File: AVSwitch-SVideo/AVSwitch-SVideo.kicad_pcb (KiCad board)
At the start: 2 copper layers, 100 x 100 mm, 9 parts, among them J1 Conn_01x35_Pin, J4 Mini-DIN-4, U1 SN74CBT3244PW

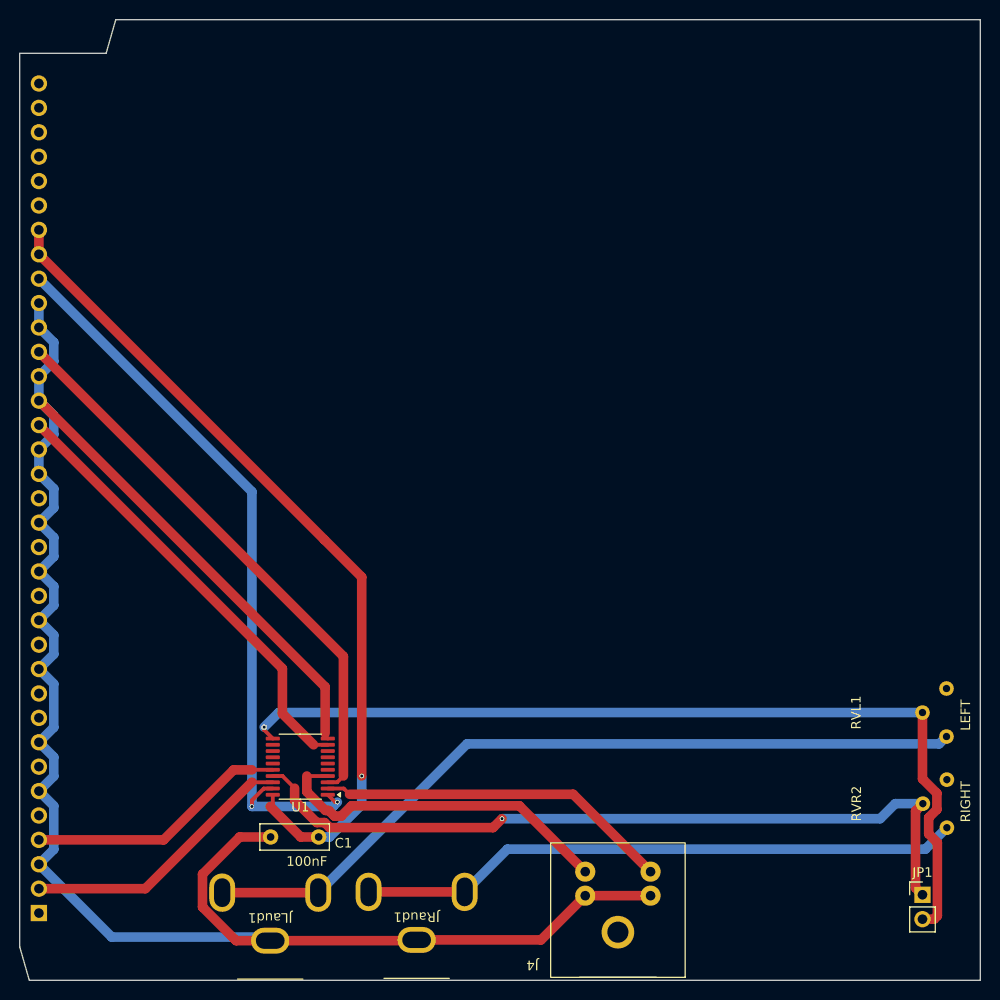
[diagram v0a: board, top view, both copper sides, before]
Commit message: Add files via upload
New version with better footprint and ground isolation.
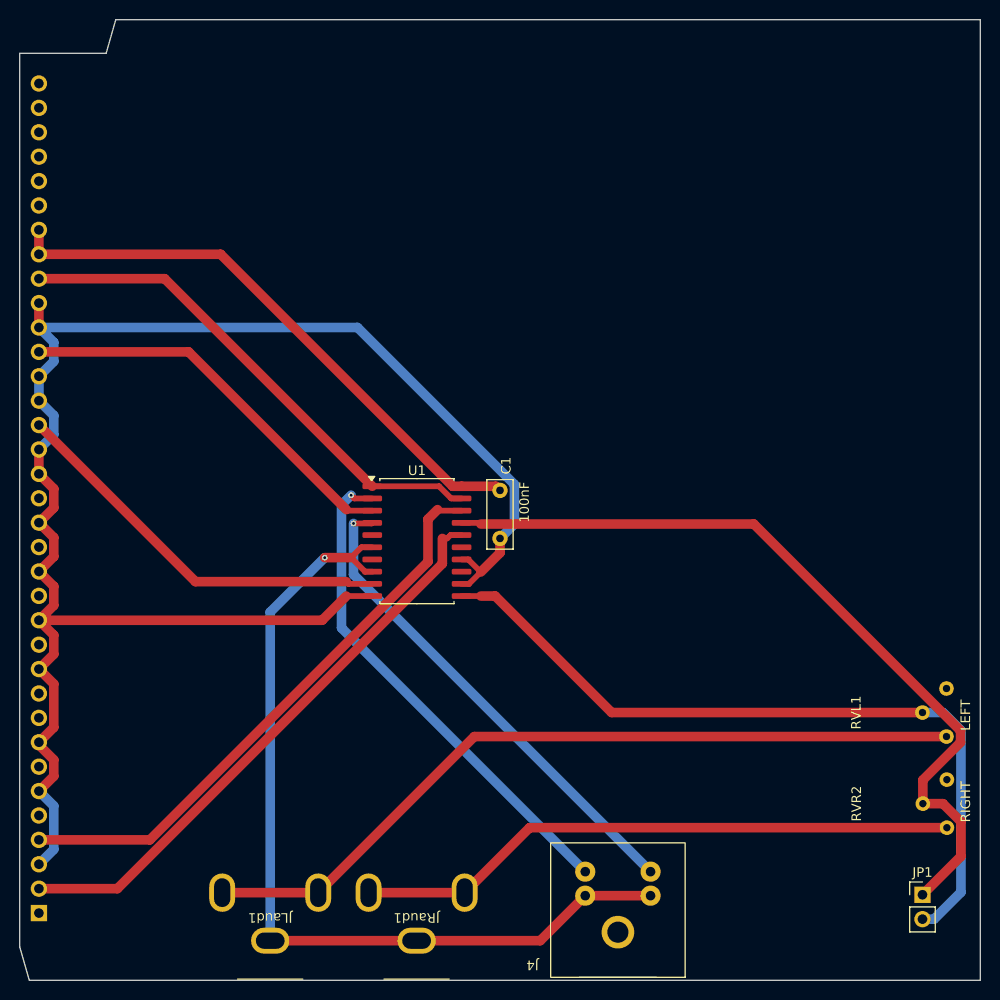
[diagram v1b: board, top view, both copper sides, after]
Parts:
- U1: footprint Package_SO:TSSOP-20_4.4x6.5mm_P0.65mm -> Package_SO:SOIC-20W_7.5x12.8mm_P1.27mm
- moved C1 40.7 mm to (156.0, 96.0), turned to -90 degrees
- moved U1 26.4 mm to (147.3, 101.3), turned to 0 degrees
- moved JRaud1 0.08 mm to (147.3, 137.9)
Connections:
- J4 pad 1: GND -> Net-(JLaud1-Ext)
- J4 pad 2: GND -> Net-(JLaud1-Ext)
- J4 pad 3: Net-(U1-1A1) -> Net-(U1-1A2)
- J4 pad 4: Net-(U1-1A2) -> Net-(U1-1A1)
- JLaud1 pad 2: GND -> Net-(JLaud1-Ext)
- JRaud1 pad 2: GND -> Net-(JLaud1-Ext)
- U1 pad 12: unconnected-(U1-1B4-Pad12) -> GND
- U1 pad 14: unconnected-(U1-1B3-Pad14) -> GND
- U1 pad 16: /SV_L -> /SV_Y
- U1 pad 18: /SV_Y -> /SV_L
- U1 pad 6: unconnected-(U1-1A3-Pad6) -> Net-(JLaud1-Ext)
- U1 pad 8: unconnected-(U1-1A4-Pad8) -> Net-(JLaud1-Ext)
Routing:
- net Net-(JLaud1-Ext): track 0.00 -> 92.0 mm, vias 0 -> 1
- net /SV_L: track 27.4 -> 60.9 mm
- net /SV_Y: track 29.0 -> 60.8 mm
- net GND: track 207.1 -> 177.6 mm
- net +5V: track 87.3 -> 60.7 mm, vias 1 -> 0
- net /ACTIVE: track 77.9 -> 53.5 mm, vias 2 -> 0
- net /R_AUD: track 59.2 -> 41.5 mm
- net Net-(U1-1A1): track 37.2 -> 52.5 mm, vias 0 -> 1
- net Net-(JP1-B): track 94.9 -> 79.8 mm, vias 1 -> 0
- net Net-(U1-1A2): track 37.1 -> 51.0 mm, vias 0 -> 1
- net /L_AUD: track 46.6 -> 41.5 mm
- net Net-(JP1-A): track 81.8 -> 84.1 mm, vias 1 -> 0
